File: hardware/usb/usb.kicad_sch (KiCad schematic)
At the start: 15 parts, among them J1 Conn_01x02, J2 Conn_01x02, J5 Conn_01x02, U1 USBLC6-2SC6, U2 AMS1117-3.3

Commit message: esp32
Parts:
- removed J1: Conn_01x02, Connector_JST:JST_ZH_S2B-ZR-SM4A-TF_1x02-1MP_P1.50mm_Horizontal, symbol Connector_Generic:Conn_01x02
- added J3: Conn_01x02, Connector_JST:JST_SHL_SM02B-SHLS-TF_1x02-1MP_P1.00mm_Horizontal, symbol Connector_Generic:Conn_01x02
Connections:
- net at U1.4 (I/O2): now also J3.1 (Pin_1)
- net at U1.6 (I/O1): now also J3.2 (Pin_2)
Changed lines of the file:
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@@
-	)
-	(symbol
-		(lib_id "Connector_Generic:Conn_01x02")
-		(at 83.82 177.8 0)
-		(unit 1)
-		(exclude_from_sim no)
-		(in_bom yes)
-		(on_board yes)
-		(dnp no)
-		(fields_autoplaced yes)
-		(property "Reference" "J1"
-			(at 86.36 177.7999 0)
-			(effects
-				(font
-					(size 1.27 1.27)
-				)
-				(justify left)
-			)
-		)
-		(property "Value" "Conn_01x02"
-			(at 86.36 180.3399 0)
-			(effects
-				(font
-					(size 1.27 1.27)
-				)
-				(justify left)
-			)
-		)
-		(property "Footprint" "Connector_JST:JST_ZH_S2B-ZR-SM4A-TF_1x02-1MP_P1.50mm_Horizontal"
-			(at 83.82 177.8 0)
-			(effects
-				(font
-					(size 1.27 1.27)
-				)
-				(hide yes)
-			)
-		)
-		(property "Datasheet" "~"
-			(at 83.82 177.8 0)
-			(effects
-				(font
-					(size 1.27 1.27)
-				)
-				(hide yes)
-			)
-		)
-		(property "Description" "Generic connector, single row, 01x02, script generated (kicad-library-utils/schlib/autogen/connector/)"
-			(at 83.82 177.8 0)
-			(effects
-				(font
-					(size 1.27 1.27)
-				)
-				(hide yes)
-			)
-		)
-		(property "LCSC" "C157930"
-			(at 83.82 177.8 0)
-			(effects
-				(font
-					(size 1.27 1.27)
-				)
-				(hide yes)
-			)
-		)
-		(pin "1"
-		)
-		(pin "2"
-		)
-		(instances
-			(project "usb"
-				(path "/9d64b1b8-57eb-4218-8a7c-add3e4ef813a"
-					(reference "J1")
-					(unit 1)
-				)
-			)
-		)
 	)
 	(symbol
@@
 					(unit 1)
 				)
+			)
+		)
+	)
+	(symbol
+		(lib_id "Connector_Generic:Conn_01x02")
+		(at 83.82 177.8 0)
+		(unit 1)
+		(exclude_from_sim no)
+		(in_bom yes)
+		(on_board yes)
+		(dnp no)
+		(fields_autoplaced yes)
+		(property "Reference" "J3"
+			(at 86.36 177.7999 0)
+			(effects
+				(font
+					(size 1.27 1.27)
+				)
+				(justify left)
+			)
+		)
+		(property "Value" "Conn_01x02"
+			(at 86.36 180.3399 0)
+			(effects
+				(font
+					(size 1.27 1.27)
+				)
+				(justify left)
+			)
+		)
+		(property "Footprint" "Connector_JST:JST_SHL_SM02B-SHLS-TF_1x02-1MP_P1.00mm_Horizontal"
+			(at 83.82 177.8 0)
+			(effects
+				(font
+					(size 1.27 1.27)
+				)
+				(hide yes)
+			)
+		)
+		(property "Datasheet" "~"
+			(at 83.82 177.8 0)
+			(effects
+				(font
+					(size 1.27 1.27)
+				)
+				(hide yes)
+			)
+		)
+		(property "Description" "Generic connector, single row, 01x02, script generated (kicad-library-utils/schlib/autogen/connector/)"
+			(at 83.82 177.8 0)
+			(effects
+				(font
+					(size 1.27 1.27)
+				)
+				(hide yes)
+			)
+		)
+		(property "LCSC" "C160402"
+			(at 83.82 177.8 0)
+			(effects
+				(font
+					(size 1.27 1.27)
+				)
+				(hide yes)
+			)
+		)
+		(pin "1"
+		)
+		(pin "2"
+		)
+		(instances
+			(project "usb"
+				(path "/9d64b1b8-57eb-4218-8a7c-add3e4ef813a"
+					(reference "J3")
+					(unit 1)
+				)

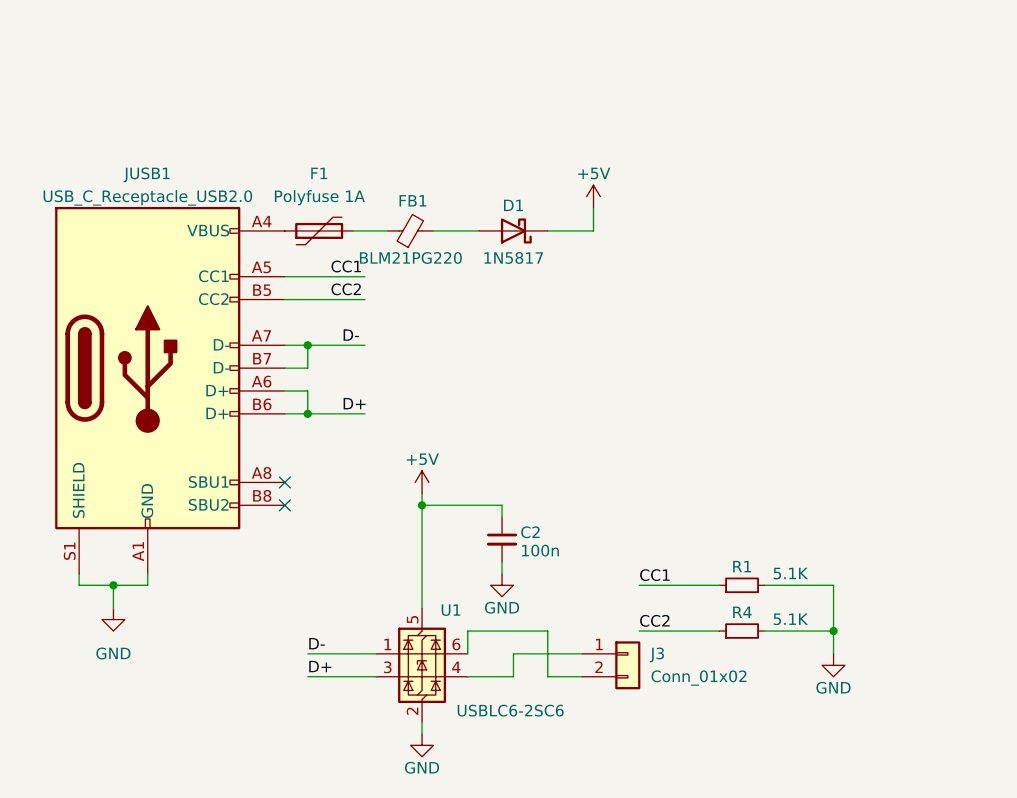
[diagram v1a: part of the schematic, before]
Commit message: simplify usb
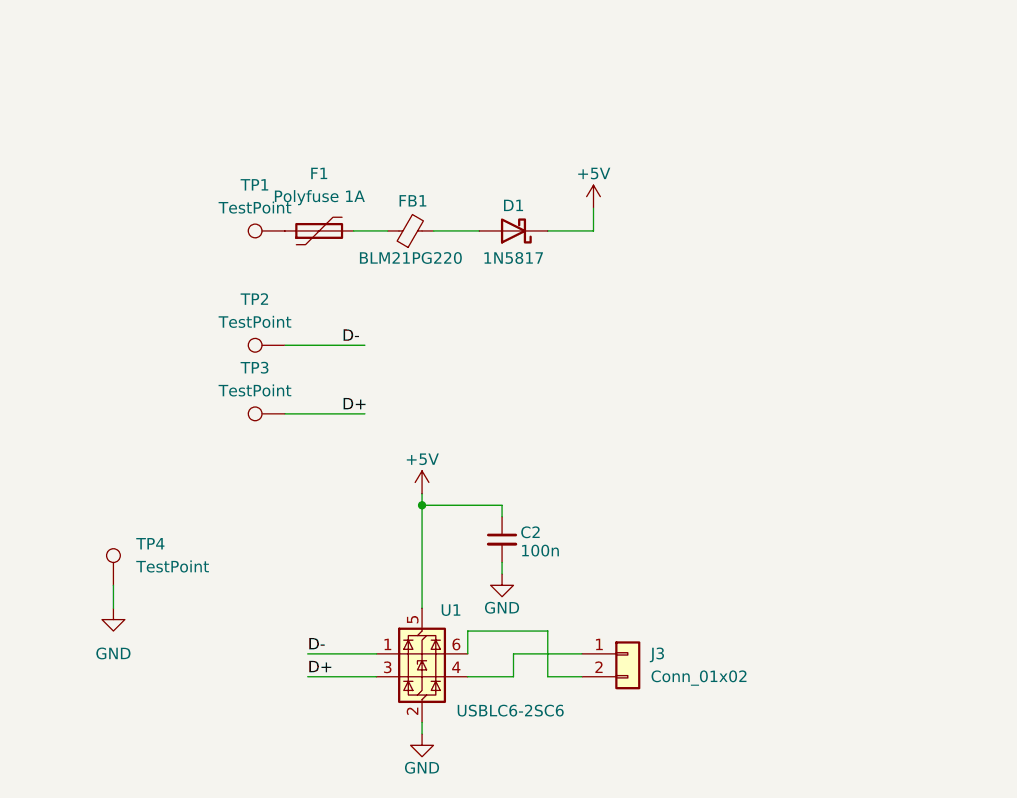
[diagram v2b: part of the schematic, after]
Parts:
- removed JUSB1: USB_C_Receptacle_USB2.0, Connector_USB:USB_C_Receptacle_GCT_USB4105-xx-A_16P_TopMnt_Horizontal, symbol Connector:USB_C_Receptacle_USB2.0
- removed R1, R4: 5.1K, Resistor_SMD:R_0402_1005Metric, symbol Morten_Library.kicad_sym_9:R_Small
- added TP1, TP2, TP3, TP4: TestPoint, TestPoint:TestPoint_Pad_1.0x1.0mm, symbol Connector:TestPoint
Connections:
- net D+: now also TP3.1
- net D-: now also TP2.1
- net GND: now also TP4.1
- net at F1.1: now also TP1.1
- no-connect marks 2 -> 0

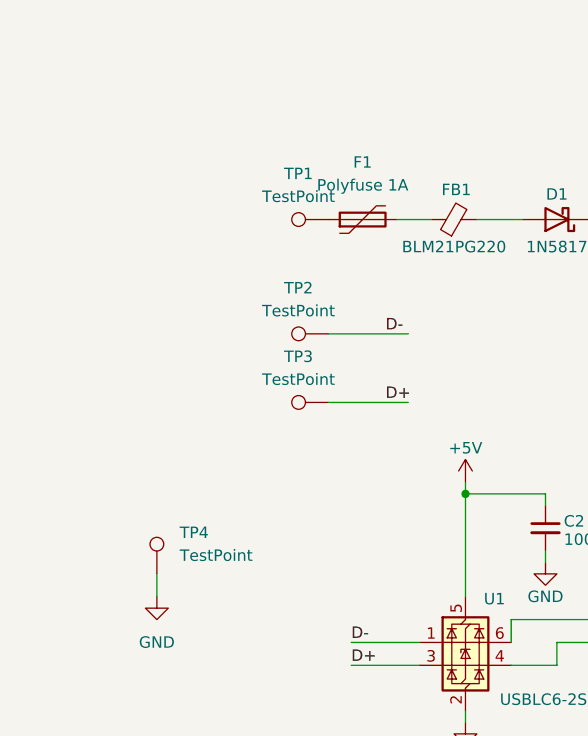
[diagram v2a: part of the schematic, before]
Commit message: simplify pins and buttons
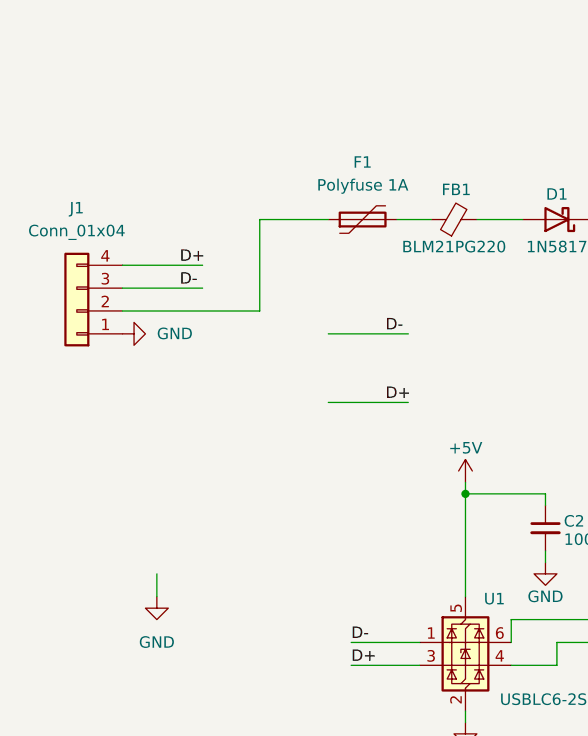
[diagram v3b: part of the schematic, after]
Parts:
- removed TP1, TP2, TP3, TP4: TestPoint, TestPoint:TestPoint_Pad_1.0x1.0mm, symbol Connector:TestPoint
- added J1: Conn_01x04, Connector_PinHeader_1.00mm:PinHeader_1x04_P1.00mm_Vertical, symbol Connector_Generic:Conn_01x04
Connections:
- net D+: now also J1.4 (Pin_4)
- net D-: now also J1.3 (Pin_3)
- net GND: now also J1.1 (Pin_1)
- net at F1.1: now also J1.2 (Pin_2)
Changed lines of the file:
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@@
+	(wire
+		(pts
+			(xy 38.1 130.81) (xy 38.1 140.97)
+		)
+		(stroke
+			(width 0)
+			(type default)
+		)
+	)
 	(wire
 		(pts
@@
 	(wire
 		(pts
+			(xy 22.86 138.43) (xy 31.75 138.43)
+		)
+		(stroke
+			(width 0)
+			(type default)
+		)
+	)
+	(wire
+		(pts
 			(xy 41.91 52.07) (xy 49.53 52.07)
 		)
@@
 	(wire
 		(pts
+			(xy 45.72 130.81) (xy 38.1 130.81)
+		)
+		(stroke
+			(width 0)
+			(type default)
+		)
+	)
+	(wire
+		(pts
 			(xy 74.93 180.34) (xy 74.93 175.26)
 		)
@@
 	(wire
 		(pts
+			(xy 22.86 135.89) (xy 31.75 135.89)
+		)
+		(stroke
+			(width 0)
+			(type default)
+		)
+	)
+	(wire
+		(pts
 			(xy 78.74 180.34) (xy 74.93 180.34)
 		)
@@
 		(pts
 			(xy 49.53 59.69) (xy 49.53 67.31)
+		)
+		(stroke
+			(width 0)
+			(type default)
+		)
+	)
+	(wire
+		(pts
+			(xy 38.1 140.97) (xy 22.86 140.97)
 		)
 		(stroke
@@
 		)
 	)
+	(label "D+"
+		(at 29.21 135.89 0)
+		(effects
+			(font
+				(size 1.27 1.27)
+			)
+			(justify left bottom)
+		)
+	)
+	(label "D-"
+		(at 29.21 138.43 0)
+		(effects
+			(font
+				(size 1.27 1.27)
+			)
+			(justify left bottom)
+		)
+	)
+	(symbol
+		(lib_id "power:GND")
+		(at 22.86 143.51 90)
+		(unit 1)
+		(exclude_from_sim no)
+		(in_bom yes)
+		(on_board yes)
+		(dnp no)
+		(fields_autoplaced yes)
+		(property "Reference" "#PWR02"
+			(at 29.21 143.51 0)
+			(effects
+				(font
+					(size 1.27 1.27)
+				)
+				(hide yes)
+			)
+		)
+		(property "Value" "GND"
+			(at 26.67 143.5099 90)
+			(effects
+				(font
+					(size 1.27 1.27)
+				)
+				(justify right)
+			)
+		)
+		(property "Footprint" ""
+			(at 22.86 143.51 0)
+			(effects
+				(font
+					(size 1.27 1.27)
+				)
+				(hide yes)
+			)
+		)
+		(property "Datasheet" ""
+			(at 22.86 143.51 0)
+			(effects
+				(font
+					(size 1.27 1.27)
+				)
+				(hide yes)
+			)
+		)
+		(property "Description" ""
+			(at 22.86 143.51 0)
+			(effects
+				(font
+					(size 1.27 1.27)
+				)
+				(hide yes)
+			)
+		)
+		(pin "1"
+		)
+		(instances
+			(project "usb"
+				(path "/9d64b1b8-57eb-4218-8a7c-add3e4ef813a"
+					(reference "#PWR02")
+					(unit 1)
+				)
+			)
+		)
+	)
 	(symbol
 		(lib_id "power:GND")
@@
 	)
 	(symbol
-		(lib_id "Connector:TestPoint")
-		(at 45.72 151.13 90)
-		(unit 1)
-		(exclude_from_sim no)
-		(in_bom yes)
-		(on_board yes)
-		(dnp no)
-		(fields_autoplaced yes)
-		(property "Reference" "TP3"
-			(at 42.418 146.05 90)
-			(effects
-				(font
-					(size 1.27 1.27)
-				)
-			)
-		)
-		(property "Value" "TestPoint"
-			(at 42.418 148.59 90)
-			(effects
-				(font
-					(size 1.27 1.27)
-				)
-			)
-		)
-		(property "Footprint" "TestPoint:TestPoint_Pad_1.0x1.0mm"
-			(at 45.72 146.05 0)
-			(effects
-				(font
-					(size 1.27 1.27)
-				)
-				(hide yes)
-			)
-		)
-		(property "Datasheet" "~"
-			(at 45.72 146.05 0)
-			(effects
-				(font
-					(size 1.27 1.27)
-				)
-				(hide yes)
-			)
-		)
-		(property "Description" "test point"
-			(at 45.72 151.13 0)
-			(effects
-				(font
-					(size 1.27 1.27)
-				)
-				(hide yes)
-			)
-		)
-		(pin "1"
-		)
-		(instances
-			(project "usb"
-				(path "/9d64b1b8-57eb-4218-8a7c-add3e4ef813a"
-					(reference "TP3")
-					(unit 1)
-				)
-			)
-		)
-	)
-	(symbol
 		(lib_id "Morten_Library.kicad_sym_9:GND")
 		(at 69.85 168.91 0)
@@
 	)
 	(symbol
-		(lib_id "Connector:TestPoint")
-		(at 45.72 143.51 90)
-		(unit 1)
-		(exclude_from_sim no)
-		(in_bom yes)
-		(on_board yes)
-		(dnp no)
-		(fields_autoplaced yes)
-		(property "Reference" "TP2"
-			(at 42.418 138.43 90)
-			(effects
-				(font
-					(size 1.27 1.27)
-				)
-			)
-		)
-		(property "Value" "TestPoint"
-			(at 42.418 140.97 90)
-			(effects
-				(font
-					(size 1.27 1.27)
-				)
-			)
-		)
-		(property "Footprint" "TestPoint:TestPoint_Pad_1.0x1.0mm"
-			(at 45.72 138.43 0)
-			(effects
-				(font
-					(size 1.27 1.27)
-				)
-				(hide yes)
-			)
-		)
-		(property "Datasheet" "~"
-			(at 45.72 138.43 0)
-			(effects
-				(font
-					(size 1.27 1.27)
-				)
-				(hide yes)
-			)
-		)
-		(property "Description" "test point"
-			(at 45.72 143.51 0)
-			(effects
-				(font
-					(size 1.27 1.27)
-				)
-				(hide yes)
-			)
-		)
-		(pin "1"
-		)
-		(instances
-			(project "usb"
-				(path "/9d64b1b8-57eb-4218-8a7c-add3e4ef813a"
-					(reference "TP2")
-					(unit 1)
-				)
-			)
-		)
-	)
-	(symbol
 		(lib_id "Device:C")
 		(at 78.74 55.88 0)
@@
 	)
 	(symbol
-		(lib_id "Connector:TestPoint")
-		(at 45.72 130.81 90)
+		(lib_id "Connector_Generic:Conn_01x04")
+		(at 17.78 140.97 180)
 		(unit 1)
 		(exclude_from_sim no)
@@
 		(dnp no)
 		(fields_autoplaced yes)
-		(property "Reference" "TP1"
-			(at 42.418 125.73 90)
-			(effects
-				(font
-					(size 1.27 1.27)
-				)
-			)
-		)
-		(property "Value" "TestPoint"
-			(at 42.418 128.27 90)
-			(effects
-				(font
-					(size 1.27 1.27)
-				)
-			)
-		)
-		(property "Footprint" "TestPoint:TestPoint_Pad_1.0x1.0mm"
-			(at 45.72 125.73 0)
+		(property "Reference" "J1"
+			(at 17.78 129.54 0)
+			(effects
+				(font
+					(size 1.27 1.27)
+				)
+			)
+		)
+		(property "Value" "Conn_01x04"
+			(at 17.78 132.08 0)
+			(effects
+				(font
+					(size 1.27 1.27)
+				)
+			)
+		)
+		(property "Footprint" "Connector_PinHeader_1.00mm:PinHeader_1x04_P1.00mm_Vertical"
+			(at 17.78 140.97 0)
 			(effects
 				(font
@@
 		)
 		(property "Datasheet" "~"
-			(at 45.72 125.73 0)
-			(effects
-				(font
-					(size 1.27 1.27)
-				)
-				(hide yes)
-			)
-		)
-		(property "Description" "test point"
-			(at 45.72 130.81 0)
-			(effects
-				(font
-					(size 1.27 1.27)
-				)
-				(hide yes)
-			)
-		)
-		(pin "1"
-		)
-		(instances
-			(project "usb"
-				(path "/9d64b1b8-57eb-4218-8a7c-add3e4ef813a"
-					(reference "TP1")
+			(at 17.78 140.97 0)
+			(effects
+				(font
+					(size 1.27 1.27)
+				)
+				(hide yes)
+			)
+		)
+		(property "Description" "Generic connector, single row, 01x04, script generated (kicad-library-utils/schlib/autogen/connector/)"
+			(at 17.78 140.97 0)
+			(effects
+				(font
+					(size 1.27 1.27)
+				)
+				(hide yes)
+			)
+		)
+		(pin "1"
+		)
+		(pin "3"
+		)
+		(pin "4"
+		)
+		(pin "2"
+		)
+		(instances
+			(project ""
+				(path "/9d64b1b8-57eb-4218-8a7c-add3e4ef813a"
+					(reference "J1")
 					(unit 1)
 				)
@@
 					(unit 1)
 				)
-			)
-		)
-	)
-	(symbol
-		(lib_id "Connector:TestPoint")
-		(at 26.67 170.18 0)
-		(unit 1)
-		(exclude_from_sim no)
-		(in_bom yes)
-		(on_board yes)
-		(dnp no)
-		(fields_autoplaced yes)
-		(property "Reference" "TP4"
-			(at 29.21 165.6079 0)
-			(effects
-				(font
-					(size 1.27 1.27)
-				)
-				(justify left)
-			)
-		)
-		(property "Value" "TestPoint"
-			(at 29.21 168.1479 0)
-			(effects
-				(font
-					(size 1.27 1.27)
-				)
-				(justify left)
-			)
-		)
-		(property "Footprint" "TestPoint:TestPoint_Pad_1.0x1.0mm"
-			(at 31.75 170.18 0)
-			(effects
-				(font
-					(size 1.27 1.27)
-				)
-				(hide yes)
-			)
-		)
-		(property "Datasheet" "~"
-			(at 31.75 170.18 0)
-			(effects
-				(font
-					(size 1.27 1.27)
-				)
-				(hide yes)
-			)
-		)
-		(property "Description" "test point"
-			(at 26.67 170.18 0)
-			(effects
-				(font
-					(size 1.27 1.27)
-				)
-				(hide yes)
-			)
-		)
-		(pin "1"
-		)
-		(instances
-			(project "usb"
-				(path "/9d64b1b8-57eb-4218-8a7c-add3e4ef813a"
-					(reference "TP4")
-					(unit 1)
-				)

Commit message: adjustments
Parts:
- added TP1, TP2, TP3, TP4: TestPoint, TestPoint:TestPoint_Pad_1.0x1.0mm, symbol Connector:TestPoint
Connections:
- net GND: now also TP1.1, TP2.1, TP3.1, TP4.1

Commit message: jlcpcb wip
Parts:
- removed TP1, TP2, TP3, TP4: TestPoint, TestPoint:TestPoint_Pad_1.0x1.0mm, symbol Connector:TestPoint
- added J4, J6, J7, J8: Conn_01x01, Connector_PinHeader_1.00mm:PinHeader_1x01_P1.00mm_Vertical, symbol Connector_Generic:Conn_01x01
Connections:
- net GND: now also J4.1 (Pin_1), J6.1 (Pin_1), J7.1 (Pin_1), J8.1 (Pin_1)

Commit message: replace connectors
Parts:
- D1: footprint Diode_SMD:D_SOD-123 -> 1N5817WS:SOD2613X110N; LCSC (none) -> C2828424
- J2, J5: footprint Connector_JST:JST_ZH_S2B-ZR-SM4A-TF_1x02-1MP_P1.50mm_Horizontal -> LIB_S2B-ZR_LF__SN_:S2BZRLFSN
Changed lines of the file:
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@@
 			)
 		)
-		(property "Footprint" "Connector_JST:JST_ZH_S2B-ZR-SM4A-TF_1x02-1MP_P1.50mm_Horizontal"
+		(property "Footprint" "LIB_S2B-ZR_LF__SN_:S2BZRLFSN"
 			(at 102.87 39.37 0)
 			(effects
@@
 			)
 		)
-		(property "Footprint" "Diode_SMD:D_SOD-123"
+		(property "Footprint" "1N5817WS:SOD2613X110N"
 			(at 71.12 126.365 0)
 			(effects
@@
 		)
 		(property "Description" "20V 1A Schottky Barrier Rectifier Diode, DO-41"
+			(at 71.12 130.81 0)
+			(effects
+				(font
+					(size 1.27 1.27)
+				)
+				(hide yes)
+			)
+		)
+		(property "LCSC" "C2828424"
 			(at 71.12 130.81 0)
 			(effects
@@
 			)
 		)
-		(property "Footprint" "Connector_JST:JST_ZH_S2B-ZR-SM4A-TF_1x02-1MP_P1.50mm_Horizontal"
+		(property "Footprint" "LIB_S2B-ZR_LF__SN_:S2BZRLFSN"
 			(at 102.87 31.75 0)
 			(effects

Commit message: fix usb connectors
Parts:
- J1: footprint Connector_PinHeader_1.00mm:PinHeader_1x04_P1.00mm_Vertical -> Connector_PinHeader_2.54mm:PinHeader_1x04_P2.54mm_Vertical
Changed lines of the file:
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@@
 			)
 		)
-		(property "Footprint" "Connector_PinHeader_1.00mm:PinHeader_1x04_P1.00mm_Vertical"
+		(property "Footprint" "Connector_PinHeader_2.54mm:PinHeader_1x04_P2.54mm_Vertical"
 			(at 17.78 140.97 0)
 			(effects
